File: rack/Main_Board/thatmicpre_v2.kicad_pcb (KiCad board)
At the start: 2 copper layers, 140 x 73.6 mm, 88 parts, among them J1 CON-SOCJ-2155, J10 Angled pinheader, J11 NCJ6FA-H, J2 NC3FBH2, J4 Female header, J5 Male pinheader, J6 Female header, J7 Male pinheader, J8 Angled pinheader, Q1 BC546CTA, Q2 BC546CTA, SW1 DPDT, SW2 DPDT, SW3 SR2612F-0112-38F5B-D8-S, U1 1512P08-U

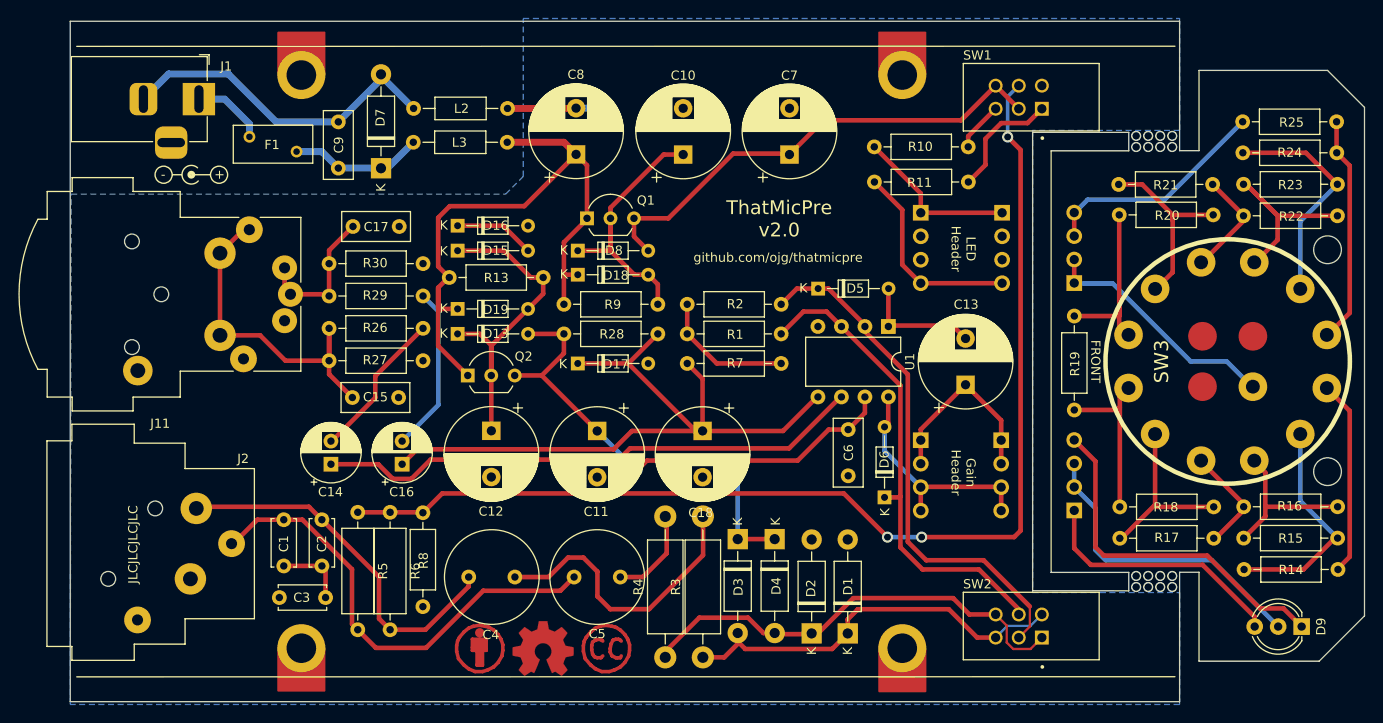
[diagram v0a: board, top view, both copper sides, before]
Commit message: Added a pad on the front panel for connecting GND to the enclosure.
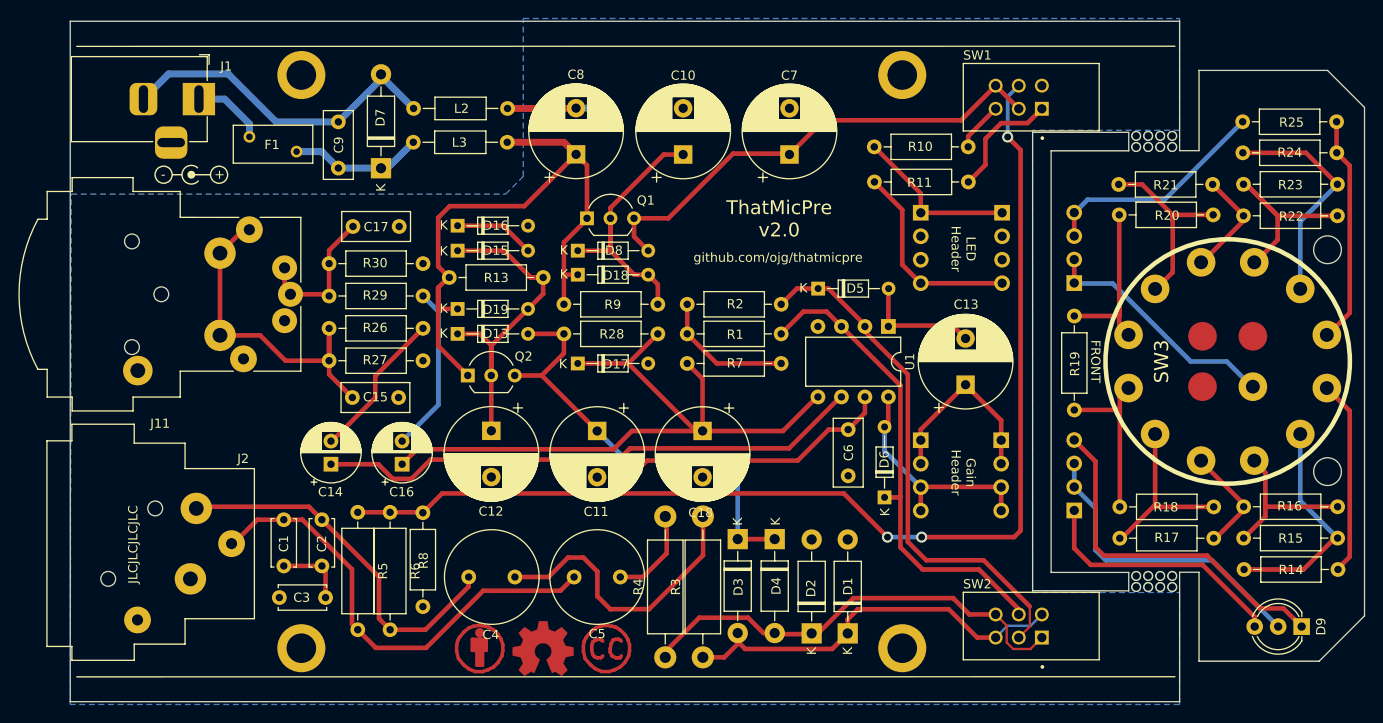
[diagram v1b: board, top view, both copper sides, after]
